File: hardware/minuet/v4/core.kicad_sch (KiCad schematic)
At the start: 19 parts, among them J6 USB4105-GF-A, J7 SM04B-SRSS-TB, SW1 EVQ-P7A01P, SW2 EVQ-P7A01P, U3 TCA9555RTW, U4 ESP32-C3-WROOM-02-N4

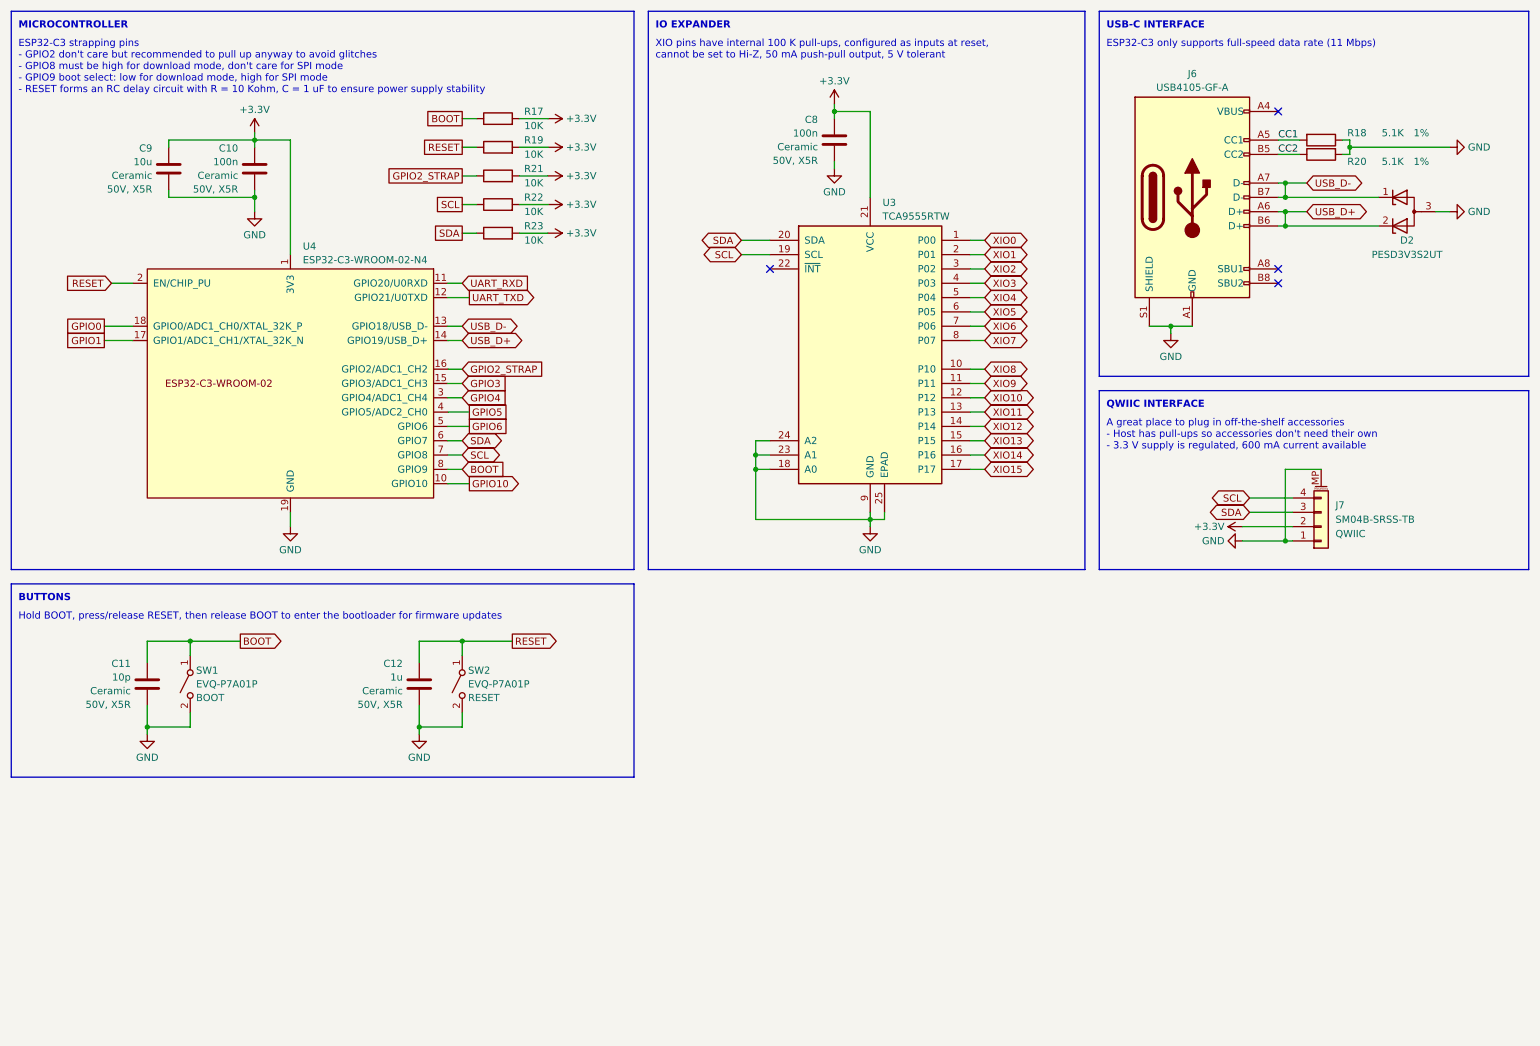
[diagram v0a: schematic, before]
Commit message: First draft of Minuet v4 fan controller board
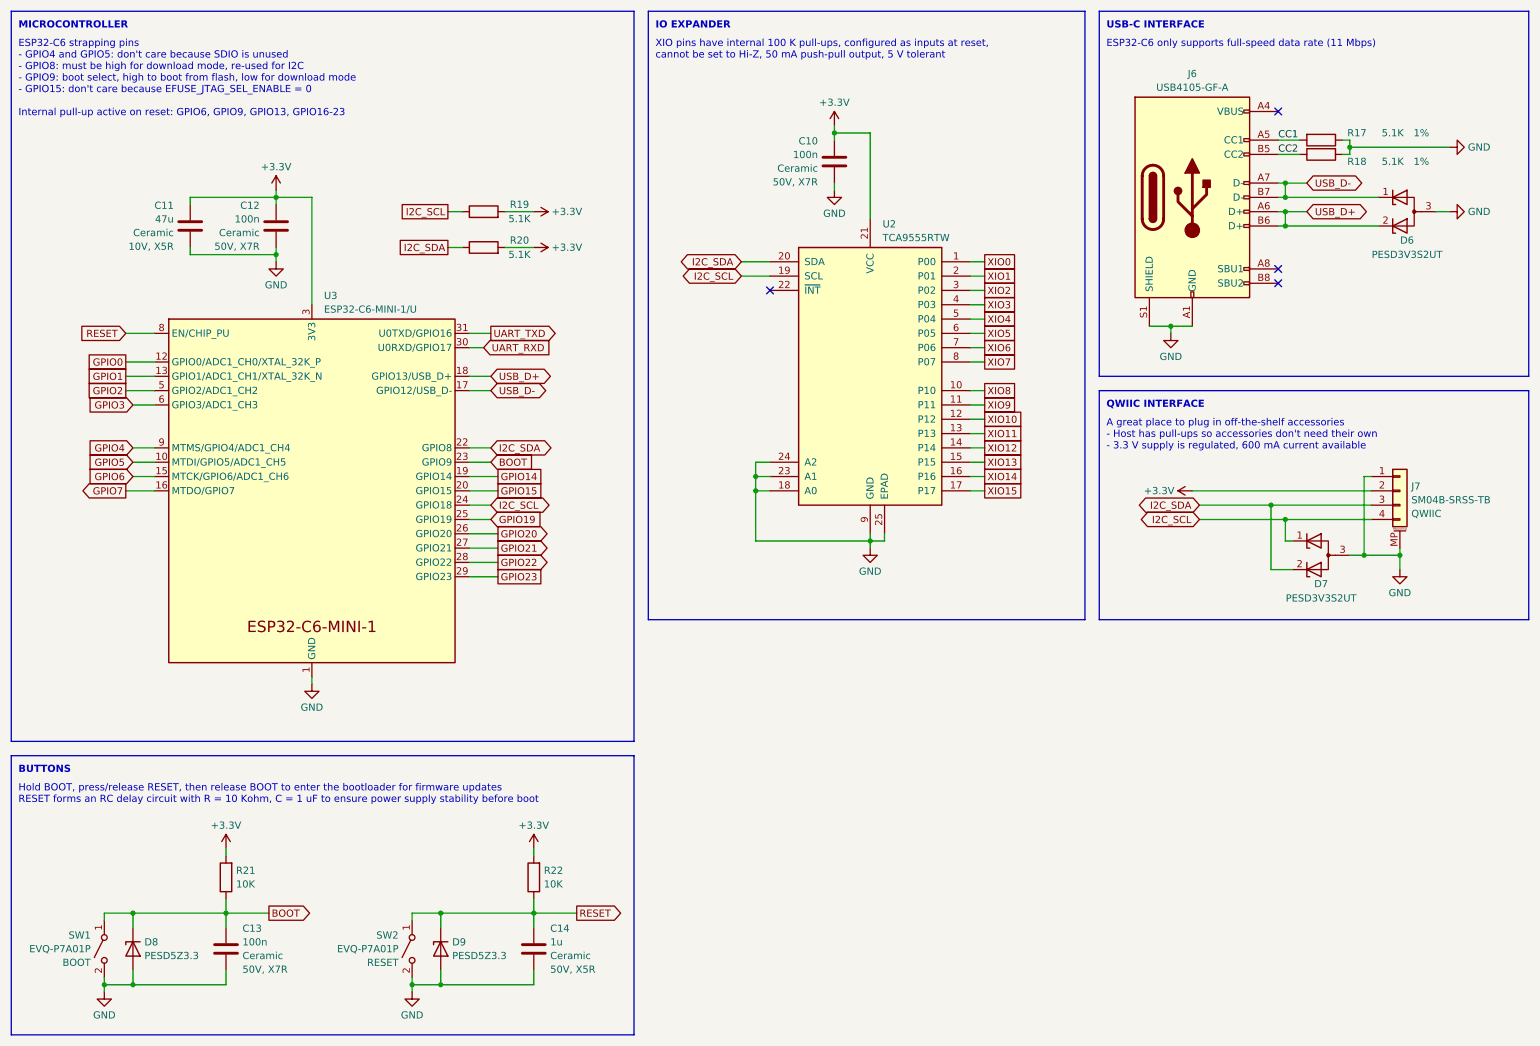
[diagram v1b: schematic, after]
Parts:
- removed C9: 10u, Capacitor_SMD:C_0805_2012Metric, symbol Device:C
- removed R21: 10K, Resistor_SMD:R_0603_1608Metric, symbol Device:R
- removed U4: ESP32-C3-WROOM-02-N4, PCM_Espressif:ESP32-C3-WROOM-02, symbol PCM_Espressif:ESP32-C3-WROOM-02
- added C11: 47u, Capacitor_SMD:C_1206_3216Metric, symbol Device:C
- added D7: PESD3V3S2UT, Package_TO_SOT_SMD:SOT-23, symbol Device:D_Zener_Dual_CommonAnode_KKA_Parallel
- added D8, D9: PESD5Z3.3, Diode_SMD:D_SOD-523, symbol Device:D_Zener
- added U3: ESP32-C6-MINI-1/U, PCM_Espressif:ESP32-C6-MINI-1, symbol PCM_Espressif:ESP32-C6-MINI-1/U
- C10: renamed from C8; Rating 50V, X5R -> 50V, X7R
- C12: renamed from C10; Rating 50V, X5R -> 50V, X7R
- C13: renamed from C11; value 10p -> 100n; LCSC C1634 -> C14663; Rating 50V, X5R -> 50V, X7R
- R19: renamed from R22; value 10K -> 5.1K; LCSC C25804 -> C23186; Rating (none) -> 1%
- R20: renamed from R23; value 10K -> 5.1K; LCSC C25804 -> C23186; Rating (none) -> 1%
- R21: renamed from R17; Rating (none) -> 1%
- R22: renamed from R19; Rating (none) -> 1%
- renumbered C12 to C14, D2 to D6, R18 to R17, R20 to R18, U3 to U2
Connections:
- net +3.3V: now also C11.1, U3.3 (3V3)
- net BOOT: now also D8.1 (K), U3.23 (GPIO9)
- net GND: now also C11.2, D7.3 (A), D8.2 (A), D9.2 (A), U3.1 (GND), U3.11 (GND), U3.14 (GND), U3.2 (GND), U3.36 (GND), U3.37 (GND), U3.38 (GND), U3.39 (GND), U3.40 (GND), U3.41 (GND), U3.42 (GND), U3.43 (GND), U3.44 (GND), U3.45 (GND), U3.46 (GND), U3.47 (GND), U3.48 (GND), U3.49 (GND), U3.50 (GND), U3.51 (GND), U3.52 (GND), U3.53 (GND)
- net GPIO0: now also U3.12 (GPIO0/ADC1_CH0/XTAL_32K_P)
- net GPIO1: now also U3.13 (GPIO1/ADC1_CH1/XTAL_32K_N)
- net GPIO3: now also U3.6 (GPIO3/ADC1_CH3)
- net GPIO4: now also U3.9 (MTMS/GPIO4/ADC1_CH4)
- net GPIO5: now also U3.10 (MTDI/GPIO5/ADC1_CH5)
- net GPIO6: now also U3.15 (MTCK/GPIO6/ADC1_CH6)
- net RESET: now also D9.1 (K), U3.8 (EN/CHIP_PU)
- net UART_RXD: now also U3.30 (U0RXD/GPIO17)
- net UART_TXD: now also U3.31 (U0TXD/GPIO16)
- net USB_D+: now also U3.18 (GPIO13/USB_D+)
- net USB_D-: now also U3.17 (GPIO12/USB_D-)
- net SCL renamed I2C_SCL
- net I2C_SCL: now also D7.1 (K), U3.24 (GPIO18)
- net SDA renamed I2C_SDA
- net I2C_SDA: now also D7.2 (K), U3.22 (GPIO8)
- new net GPIO14: U3.19 (GPIO14)
- new net GPIO15: U3.20 (GPIO15)
- new net GPIO19: U3.25 (GPIO19)
- new net GPIO2: U3.5 (GPIO2/ADC1_CH2)
- new net GPIO20: U3.26 (GPIO20)
- new net GPIO21: U3.27 (GPIO21)
- new net GPIO22: U3.28 (GPIO22)
- new net GPIO23: U3.29 (GPIO23)
- new net GPIO7: U3.16 (MTDO/GPIO7)
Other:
- note added: "ESP32-C6 only supports full-speed data rate (11 Mbps)"
- note added: "ESP32-C6 strapping pins - GPIO4 and GPIO5: don't care because SDIO is unused - GPIO8: must be high for download mode, re-used for I2C - GPIO9: boot select, high to boot from flash, low for download mode - GPIO15: don't care because EFUSE_JTAG_SEL_ENABLE = 0 Internal pull-up active on reset: GPIO6, GPIO9, GPIO13, GPIO16-23"
- note added: "Hold BOOT, press/release RESET, then release BOOT to enter the bootloader for firmware updates RESET forms an RC delay circuit with R = 10 Kohm, C = 1 uF to ensure power supply stability before boot"
- note removed: "ESP32-C3 only supports full-speed data rate (11 Mbps)"
- note removed: "ESP32-C3 strapping pins - GPIO2 don't care but recommended to pull up anyway to avoid glitches - GPIO8 must be high for download mode, don't care for SPI mode - GPIO9 boot select: low for download mode, high for SPI mode - RESET forms an RC delay circuit with R = 10 Kohm, C = 1 uF to ensure power supply stability"
- note removed: "Hold BOOT, press/release RESET, then release BOOT to enter the bootloader for firmware updates"
- company: (none) -> Brown Studios LLC
- title: Minuet Core -> Minuet Core Logic
- moved on the sheet: C10, C12, C13, C14, J7, R19, R20, R21, R22, SW1, SW2, U2

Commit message: Second draft of Minuet v4 main board.
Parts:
- R20: renamed from R19; value 5.1K -> 3.3K; LCSC C23186 -> C22978
- R21: renamed from R20; value 5.1K -> 3.3K; LCSC C23186 -> C22978
- U3: FT Origin (none) -> Center
- renumbered C10 to C11, C11 to C12, C12 to C13, C13 to C14, C14 to C15, R17 to R18, R18 to R19, R21 to R22, R22 to R23
